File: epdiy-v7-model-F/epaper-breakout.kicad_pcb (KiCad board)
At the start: 4 copper layers, 100 x 55 mm, 111 parts, among them J2 EXTENSION_HEADER, J3 SM04B-SRSS-TB_LF__SN_, J4 XF2M-3315-1A, J5 CONN_BAT, J6 8BIT_HEADER, J7 ESP_HDR, J8 ED133UT2, J9 USB_C_Receptacle_USB2.0, Q1 AO3401A, U1 MCP1700-3302E_SOT23, U10 RT9080-33GJ5, U11 TP4056, U2 PCA9535PW, U3 TPS651851RSLR, U6 ED078KH6, U8 ESP32-S3-WROOM-1, Y1 RV-3032-C7

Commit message: Starting to accomodate stuff over the board
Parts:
- removed C18: 1uF, Capacitor_SMD:C_0805_2012Metric
- removed C19: 10uF, Capacitor_SMD:C_0805_2012Metric
- removed J2: EXTENSION_HEADER, Connector_PinHeader_2.54mm:PinHeader_1x12_P2.54mm_Vertical
- removed J7: ESP_HDR, Connector_PinHeader_2.54mm:PinHeader_1x08_P2.54mm_Vertical
- removed J8: ED133UT2, epaper-breakout:HRS_FH26W-39S-0.3SHW(60)
- removed JP1: VBAT_GPIO2, Jumper:SolderJumper-2_P1.3mm_Bridged2Bar_Pad1.0x1.5mm
- removed JP2: RTCINT_GPIO2, Jumper:SolderJumper-2_P1.3mm_Bridged2Bar_Pad1.0x1.5mm
- removed TP6: RTC_CLK, TestPoint:TestPoint_Pad_D1.5mm
- U6: footprint footprints:FH1240S05SH55 -> epaper-breakout:Hirose_FH12-40S-0.5SH_mirrored
- moved J3 117.8 mm to (22.5, 115.4), turned to -90 degrees
- moved H3 113.4 mm to (56.0, 166.4)
- moved JP3 103.6 mm to (32.5, 119.4)
- moved R32 103.3 mm to (86.3, 144.0), turned to 0 degrees
- moved C41 99.3 mm to (83.9, 157.9)
- moved Y1 98.4 mm to (86.4, 140.3)
- moved C43 98.4 mm to (85.9, 134.7)
- moved C21 97.9 mm to (38.7, 118.6)
- moved U10 97.9 mm to (40.3, 114.6)
- moved R27 97.0 mm to (85.2, 120.1), turned to 45 degrees
- moved U8 96.4 mm to (71.5, 152.7)
- moved C33 96.3 mm to (25.9, 155.8), turned to 0 degrees
- moved C35 96.1 mm to (86.4, 121.7), turned to 45 degrees
- moved C39 95.7 mm to (40.2, 110.8), turned to 180 degrees
- moved C17 95.2 mm to (87.8, 157.6)
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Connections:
- U2 pad 10: /EXT7 -> unconnected-(U2-IO0_6-Pad10)
- U2 pad 11: /EXT8 -> unconnected-(U2-IO0_7-Pad11)
- U2 pad 4: /EXT1 -> unconnected-(U2-IO0_0-Pad4)
- U2 pad 5: /EXT2 -> unconnected-(U2-IO0_1-Pad5)
- U2 pad 6: /EXT3 -> unconnected-(U2-IO0_2-Pad6)
- U2 pad 7: /EXT4 -> unconnected-(U2-IO0_3-Pad7)
- U2 pad 8: /EXT5 -> unconnected-(U2-IO0_4-Pad8)
- U2 pad 9: /EXT6 -> unconnected-(U2-IO0_5-Pad9)
- U8 pad 10: /D5 -> /D10
- U8 pad 11: /D6 -> /D9
- U8 pad 12: /D7 -> /D8
- U8 pad 17: /D8 -> /D7
- U8 pad 18: /D9 -> /D6
- U8 pad 19: /D10 -> /D5
- U8 pad 20: /D11 -> /D4
- U8 pad 21: /D12 -> /D3
- U8 pad 22: /D13 -> /D2
- U8 pad 23: /D14 -> /D1
- U8 pad 24: /D15 -> /D0
- U8 pad 25: /CKV -> /LEH
- U8 pad 26: /EP_STV -> /XSTL
- U8 pad 31: /~{GPIO_INTR} -> /GPIO_38
- U8 pad 34: /XSTL -> /EP_STV
- U8 pad 35: /LEH -> /CKV
- U8 pad 38: /GPIO_2 -> /~{GPIO_INTR}
- U8 pad 5: /D0 -> /D15
- U8 pad 6: /D1 -> /D14
- U8 pad 7: /D2 -> /D13
- U8 pad 8: /D3 -> /D12
- U8 pad 9: /D4 -> /D11
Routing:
- net /-20V: track 216.9 -> 16.2 mm, vias 7 -> 2
- net EPD_VDD: track 161.4 -> 13.5 mm, vias 5 -> 1
- net /+22V: track 206.1 -> 60.3 mm, vias 6 -> 3
- net /SDA: track 155.1 -> 22.1 mm, vias 5 -> 3
- net /15V: track 200.4 -> 69.3 mm, vias 9 -> 3
- net /EP_VCOM: track 165.1 -> 38.3 mm, vias 7 -> 2
- net /-15V: track 181.8 -> 57.3 mm, vias 6 -> 1
- net /EP_MODE: track 109.2 -> 0.00 mm, vias 7 -> 0
- net /ESP_USB+: track 101.9 -> 0.00 mm, vias 2 -> 0
- net /SCL: track 123.6 -> 21.9 mm, vias 4 -> 2
- net /EP_OE: track 99.8 -> 0.00 mm, vias 6 -> 0
- net /ESP_USB-: track 101.9 -> 3.33 mm, vias 2 -> 0
- net /EN: track 99.2 -> 2.13 mm, vias 4 -> 0
- net GND: track 189.1 -> 94.0 mm, vias 104 -> 64
- net /CKV: track 81.8 -> 0.00 mm, vias 7 -> 0
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- removed copper zone on In2.Cu, net 3.3V
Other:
- board size 100 x 55 mm -> 67.7 x 82.7 mm
- board text added: "40pin, 16bit EPD 10.3{dblquote}"
- board text added: "HIGH ▲ for 3V3 I2C QWIIC"
- board text added: "IO 46"
- board text added: "▼ LIPO BATT."
- board text removed: "1"
- board text removed: "3.3V"
- board text removed: "39pin, 8bit ED133UT*"
- board text removed: "40"
- board text removed: "40pin, 16bit EPD"
- board text removed: "D10"
- board text removed: "D11"
- board text removed: "D12"
- board text removed: "D13"
- board text removed: "D14"
- board text removed: "D15"
- board text removed: "D8"
- board text removed: "D9"
- board text removed: "EN"
- board text removed: "EPD3.3V"
- board text removed: "EXT1"
- board text removed: "EXT2"
- board text removed: "EXT3"
- board text removed: "EXT4"
- board text removed: "EXT5"
- board text removed: "EXT6"
- board text removed: "EXT7"
- board text removed: "EXT8"
- board text removed: "GND"
- board text removed: "HIGH ▲ for 3V3 extra power"
- board text removed: "IO0"
- board text removed: "IO1"
- board text removed: "IO2"
- board text removed: "IO3"
- board text removed: "IO46"
- board text removed: "Joins U10 500mA ▴ w/general 3V3"
- board text removed: "RTC CLK"
- board text removed: "RTCI-IO2"
- board text removed: "Rel 1.1.1 PCB custom modified for 9.7, 13.3 inch displays (8 bit)"
- board text removed: "SCL"
- board text removed: "SDA"
- board text removed: "VBAT-IO1"
- board text removed: "epdiy v7 by Valentin Roland 2023 Thanks to the epdiy contributors! For sources and documentation visit https://github.com/vroland/epdiy"
- board text removed: "epdiy v7_10.3{dblquote}"
- board text removed: "▲"

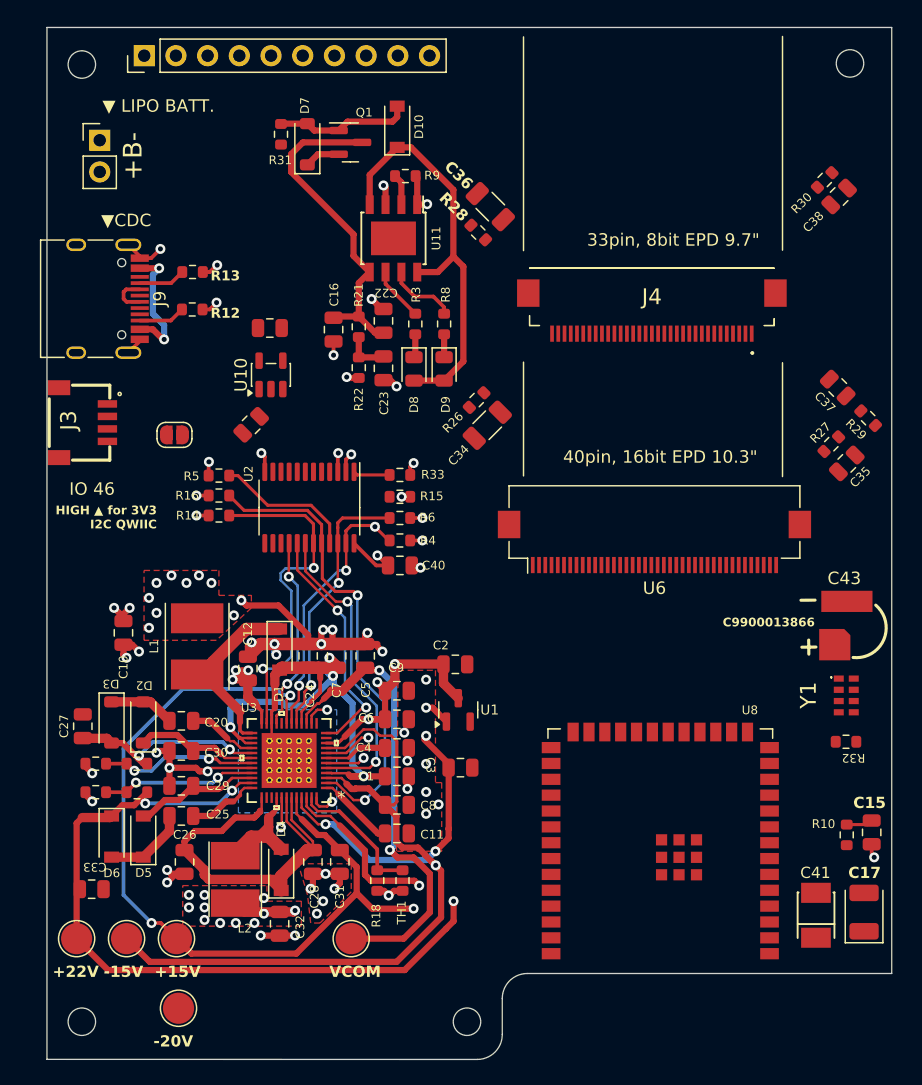
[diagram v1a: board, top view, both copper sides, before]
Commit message: DRC validation missing
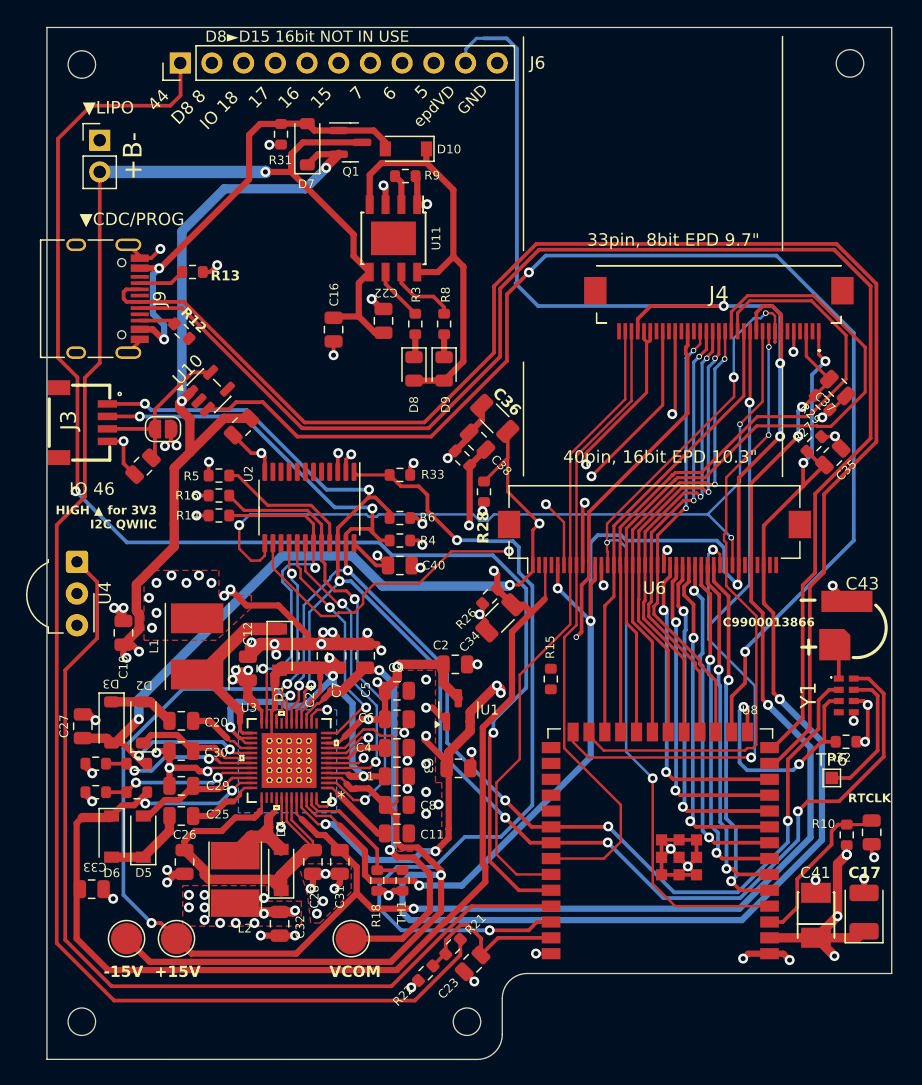
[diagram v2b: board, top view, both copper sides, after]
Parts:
- removed TP1: +22V, TestPoint:TestPoint_Pad_D2.5mm
- removed TP3: -20V, TestPoint:TestPoint_Pad_D2.5mm
- added TP6: RTC_CLK, TestPoint:TestPoint_Pad_1.0x1.0mm, F.Cu at (85.2, 146.9)
- added U4: TSOP341xx, OptoDevice:Vishay_MOLD-3Pin, F.Cu at (24.7, 129.6)
- J6: footprint Connector_PinHeader_2.54mm:PinHeader_1x10_P2.54mm_Vertical -> Connector_PinHeader_2.54mm:PinHeader_1x11_P2.54mm_Vertical
- R22: value 150k -> 680k
- moved R21 50.2 mm to (54.9, 160.4), turned to -135 degrees
- moved R22 48.8 mm to (52.7, 162.5), turned to -135 degrees
- moved C23 48.2 mm to (56.4, 161.7), turned to 45 degrees
- moved R30 36.6 mm to (55.6, 121.3), turned to 135 degrees
- moved C38 35.0 mm to (56.8, 119.9), turned to 135 degrees
- moved R28 20.8 mm to (57.3, 123.9), turned to -90 degrees
- moved R15 19.0 mm to (62.7, 138.9), turned to 90 degrees
- moved C36 17.0 mm to (58.2, 118.1)
- moved R26 15.8 mm to (57.8, 132.3)
- moved C34 15.5 mm to (58.6, 134.0)
- moved C39 15.0 mm to (30.0, 121.9), turned to 45 degrees
- moved J4 5.37 mm to (76.2, 108.1)
- moved U10 5.13 mm to (35.3, 115.9), turned to 45 degrees
- moved R29 3.86 mm to (84.5, 116.8)
- moved J6 2.94 mm to (33.0, 89.6)
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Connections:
- net 3.3V renamed +3V3
- net QWIIC_3V3 renamed +3V3_QW
- C23 pad 2: Net-(JP1-B) -> /GPIO_1
- J4 pad 33: /BORDER -> unconnected-(J4-BORDER-Pad33)
- J6 pad 1: /D8 -> /GPIO_44
- J6 pad 10: GND -> EPD_VDD
- J6 pad 2: /D9 -> /D8
- J6 pad 3: /D10 -> /D9
- J6 pad 4: /D11 -> /D10
- J6 pad 5: /D12 -> /D11
- J6 pad 6: /D13 -> /D12
- J6 pad 7: /D14 -> /D13
- J6 pad 8: /D15 -> /D14
- J6 pad 9: EPD_VDD -> /D15
- R21 pad 2: Net-(JP1-B) -> /GPIO_1
- R22 pad 1: Net-(JP1-B) -> /GPIO_1
- R32 pad 1: /RTC_INT -> /GPIO_3
- U6 pad 40: /BORDER -> Net-(U6-BORDER)
- U8 pad 36: /USB_TXD -> /GPIO_44
- U8 pad 37: /USB_RXD -> /IR_OUT
- Y1 pad 3: /RTC_INT -> /GPIO_3
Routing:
- net EPD_VDD: track 13.5 -> 159.8 mm, vias 1 -> 7
- net /ESP_USB-: track 3.33 -> 119.2 mm
- net +BATT: track 26.6 -> 142.4 mm, vias 0 -> 1
- net /ESP_USB+: track 0.00 -> 113.4 mm
- net /GPIO_44: track 0.00 -> 111.2 mm, vias 0 -> 2
- net /GPIO_46: track 0.00 -> 100.9 mm, vias 0 -> 2
- net /SCL: track 21.9 -> 120.2 mm, vias 2 -> 7
- net /SDA: track 22.1 -> 113.3 mm, vias 3 -> 7
- net /-15V: track 57.3 -> 148.5 mm, vias 1 -> 4
- net /15V: track 69.3 -> 149.5 mm, vias 3 -> 6
- net /-20V: track 16.2 -> 95.6 mm, vias 2 -> 6
- net /IR_OUT: track 0.00 -> 75.1 mm
- net /XCL: track 0.00 -> 68.5 mm, vias 0 -> 4
- net /~{GPIO_INTR}: track 2.95 -> 69.1 mm, vias 0 -> 2
- net /EP_OE: track 0.00 -> 65.3 mm, vias 0 -> 3
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- added copper zone on In2.Cu, net +3V3
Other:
- board text added: "15"
- board text added: "16"
- board text added: "17"
- board text added: "44"
- board text added: "5"
- board text added: "6"
- board text added: "7"
- board text added: "D8 8"
- board text added: "D8►D15 16bit NOT IN USE"
- board text added: "GND"
- board text added: "IO 18"
- board text added: "RTCLK"
- board text added: "epdVD"
- board text added: "▼CDC/PROG"
- board text added: "▼LIPO"
- board text removed: "+22V"
- board text removed: "-20V"
- board text removed: "▼ LIPO BATT."
- board text removed: "▼CDC"

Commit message: First model routed
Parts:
- added C42: 22pF, Capacitor_SMD:C_0402_1005Metric, F.Cu at (26.7, 138.1)
- added SW2: HX-3X6X3.5-CA-0.6-2.5N, footprint_common:C2686860_button_TC073B-H055-L1, F.Cu at (24.3, 138.1)
- added SW3: HX-3X6X3.5-CA-0.6-2.5N, footprint_common:C2686860_button_TC073B-H055-L1, F.Cu at (24.3, 95.8)
- moved JP3 5.85 mm to (30.9, 124.7), turned to -90 degrees
- moved J5 1.98 mm to (28.5, 95.8)
- moved U4 0.79 mm to (24.7, 128.8)
- moved R15 0.79 mm to (62.0, 139.3), turned to 180 degrees
- moved C39 0.76 mm to (30.3, 121.2)
- moved R28 0.72 mm to (56.9, 124.5)
- moved H1 0.66 mm to (86.7, 90.3)
- moved H4 0.66 mm to (25.2, 90.4)
- moved R26 0.42 mm to (57.5, 132.6)
- moved C27 0.39 mm to (25.2, 143.1)
- moved C34 0.20 mm to (58.6, 134.2)
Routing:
- net /EN: track 13.5 -> 128.6 mm
- net /D11: track 27.6 -> 114.2 mm
- net /D13: track 28.2 -> 97.2 mm
- net /D9: track 26.0 -> 93.1 mm
- net /D8: track 25.5 -> 92.2 mm
- net /D10: track 26.9 -> 93.3 mm
- net /D15: track 29.7 -> 92.5 mm
- net /D14: track 28.6 -> 91.2 mm
- net /D12: track 27.5 -> 88.6 mm
- net /IO0: track 0.00 -> 46.5 mm, vias 0 -> 2
- net GND: track 154.3 -> 160.9 mm
- net /ESP_USB+: track 113.4 -> 117.1 mm
- net +3V3_QW: track 13.5 -> 17.0 mm
- net /IR_OUT: track 75.1 -> 78.2 mm
- net +3V3: track 74.5 -> 76.2 mm, vias 19 -> 18
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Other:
- outline, holes or cut-outs redrawn
- board text added: "BOOT"
- board text added: "D15 5"
- board text added: "IO 17"
- board text added: "▲LIPO"
- board text added: "▲RST"
- board text added: "►IR"
- board text added: "►RTCLK"
- board text removed: "17"
- board text removed: "5"
- board text removed: "RTCLK"
- board text removed: "▼LIPO"

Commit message: Update 33 pin w/34 and add 2nd USBC
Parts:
- removed J4: XF2M-3315-1A, footprints:FH1233S05SH55
- added J10: USB_C_Receptacle_USB2.0, Connector_USB:USB_C_Receptacle_HRO_TYPE-C-31-M-12, F.Cu at (87.2, 98.2)
- added U12: ED060XC5, footprint_common:X05A20H34G, F.Cu at (74.2, 110.8)
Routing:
- net VBUS: track 35.8 -> 79.6 mm, vias 2 -> 4
- net /-20V: track 94.2 -> 114.6 mm, vias 6 -> 7
- net /15V: track 149.5 -> 167.3 mm, vias 6 -> 7
- net /ESP_USB+: track 117.1 -> 133.8 mm, vias 0 -> 2
- net /D0: track 36.7 -> 53.3 mm
- net /ESP_USB-: track 119.6 -> 134.0 mm, vias 0 -> 2
- net EPD_VDD: track 159.9 -> 147.3 mm
- net GND: track 160.9 -> 173.3 mm, vias 87 -> 91
- net /D2: track 58.4 -> 64.6 mm
- net /CKV: track 50.2 -> 56.3 mm
- net /+22V: track 122.8 -> 117.6 mm
- net /XCL: track 67.6 -> 63.6 mm, vias 4 -> 2
- net /D1: track 54.7 -> 58.1 mm
- net /EN: track 128.6 -> 130.1 mm
- net /EP_MODE: track 53.9 -> 52.6 mm
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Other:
- board text added: "34pin, 8bit EPD 6{dblquote}"
- board text removed: "33pin, 8bit EPD 9.7{dblquote}"

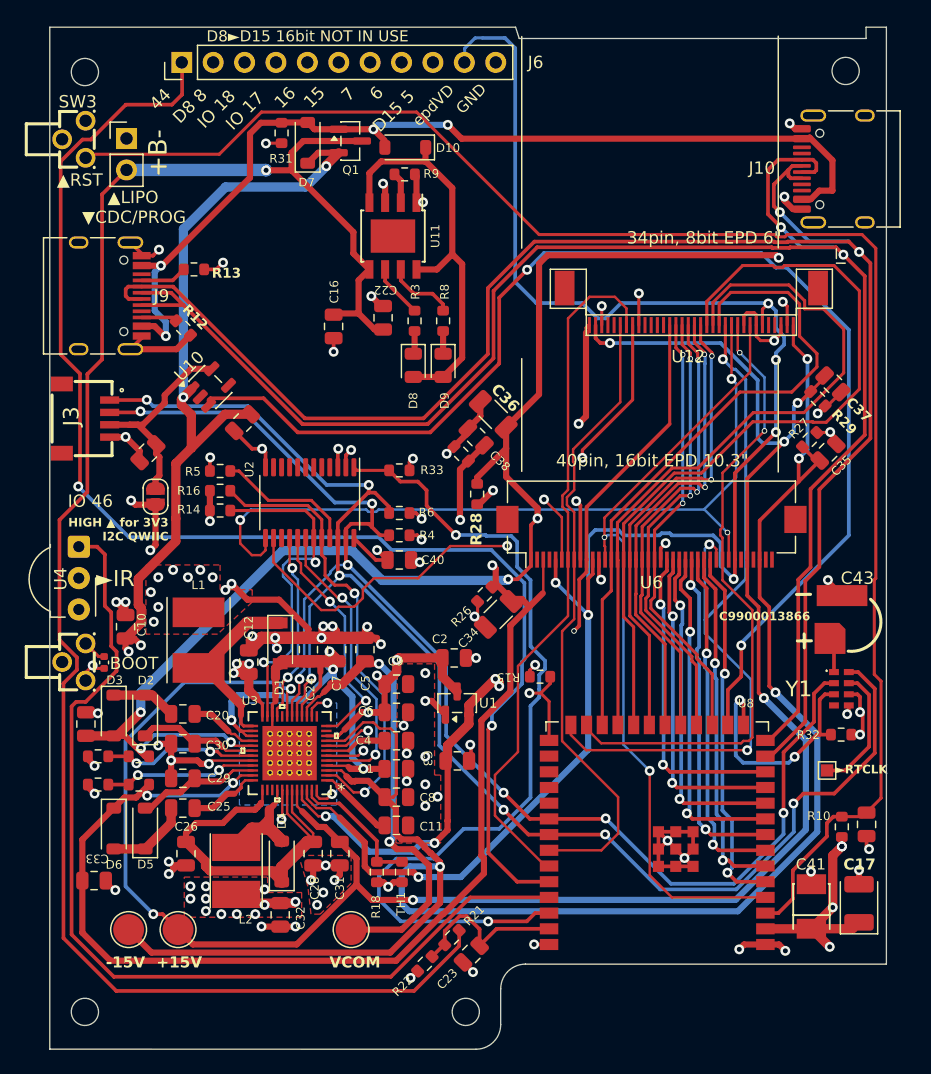
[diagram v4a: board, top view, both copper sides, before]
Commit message: Round corners + better USBC location
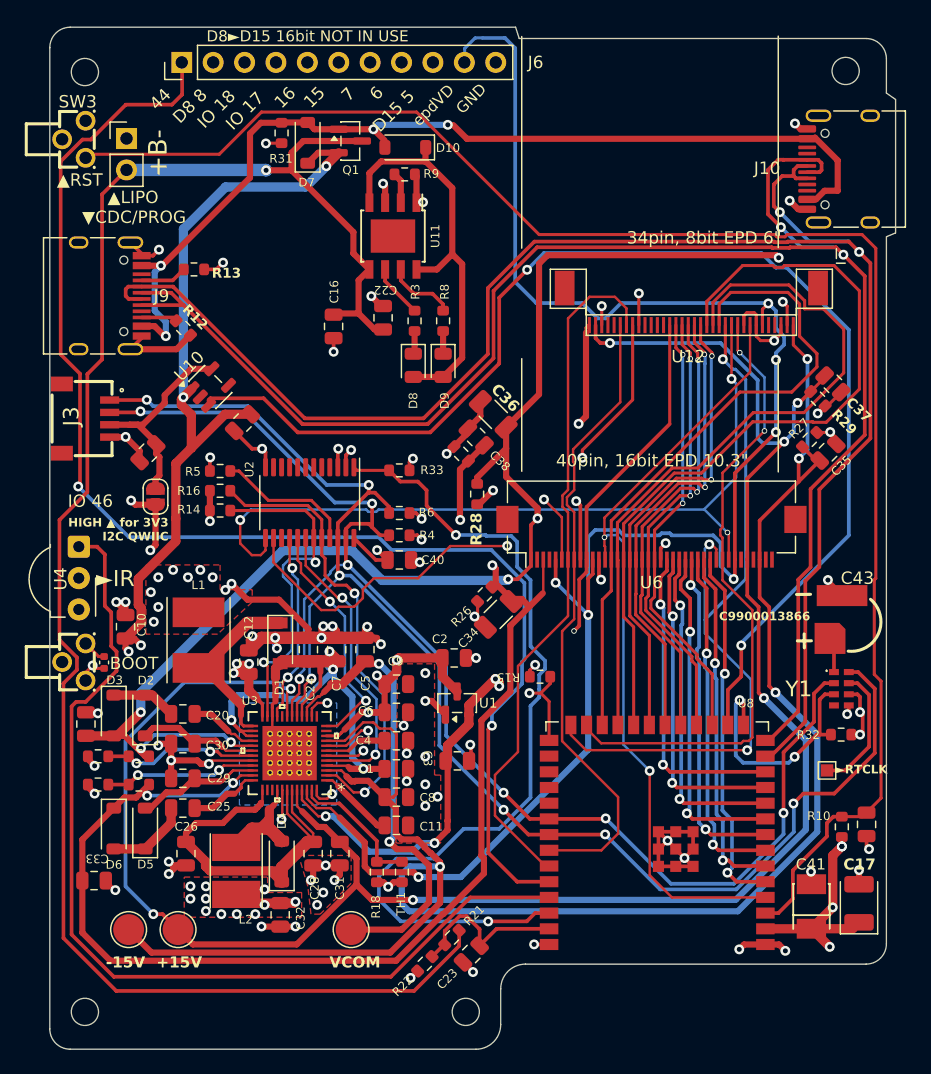
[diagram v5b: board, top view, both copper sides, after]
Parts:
- moved J10 0.43 mm to (87.6, 98.2)
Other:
- board size 67.7 x 82.7 mm -> 68.4 x 82.7 mm
